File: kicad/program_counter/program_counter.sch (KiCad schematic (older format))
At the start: 34 parts, among them J1 DB37_Male, U76 SN74ALVC00

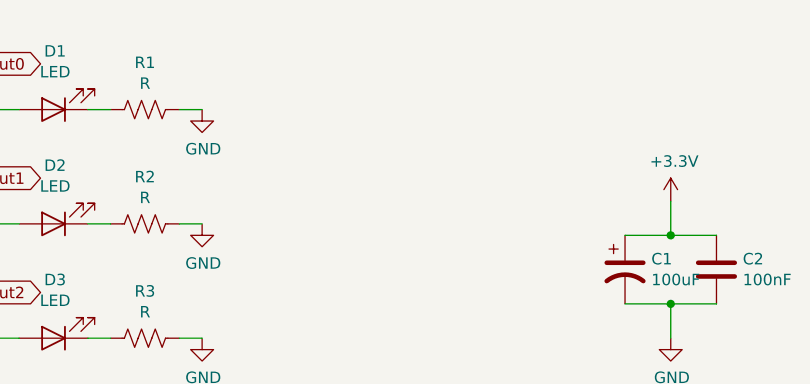
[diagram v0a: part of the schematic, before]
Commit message: ALU schematic, layout, routing complete. Associated motherboardmod. Also added Load LED to register and program counter boards.
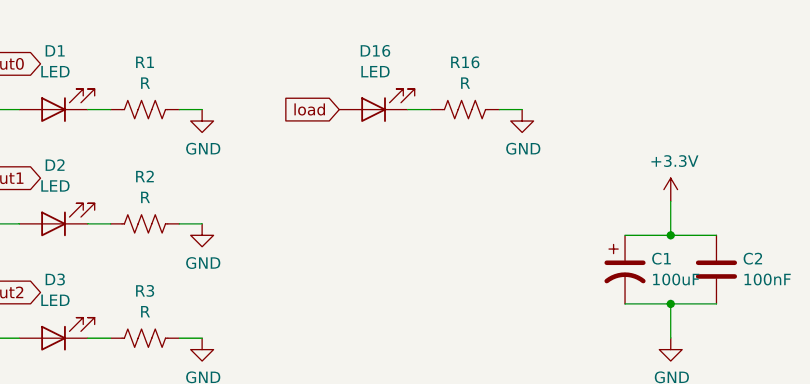
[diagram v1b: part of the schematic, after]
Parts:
- added D16: LED, LED_THT:LED_D5.0mm, symbol Device:LED
- added R16: R, Resistor_SMD:R_1206_3216Metric, symbol Device:R_US
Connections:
- net GND: now also R16.1
- net load: now also D16.2 (A)
- new net: D16.1 (K), R16.2
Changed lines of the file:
@@
 Wire Wire Line
 	7800 3350 7800 3200
+$Comp
+L Device:LED D16
+U 1 1 5EB18DDF
+P 6450 900
+F 0 "D16" H 6443 645 50  0000 C CNN
+F 1 "LED" H 6443 736 50  0000 C CNN
+F 2 "LED_THT:LED_D5.0mm" H 6450 900 50  0001 C CNN
+F 3 "~" H 6450 900 50  0001 C CNN
+	1    6450 900
+	-1   0    0    1
+$EndComp
+$Comp
+L Device:R_US R16
+U 1 1 5EB18DE5
+P 6850 900
+F 0 "R16" V 6645 900 50  0000 C CNN
+F 1 "R" V 6736 900 50  0000 C CNN
+F 2 "Resistor_SMD:R_1206_3216Metric" V 6780 900 50  0001 C CNN
+F 3 "~" H 6850 900 50  0001 C CNN
+	1    6850 900
+	0    1    1    0
+$EndComp
+Wire Wire Line
+	6600 900  6700 900
+$Comp
+L power:GND #PWR0172
+U 1 1 5EB18DEC
+P 7100 900
+F 0 "#PWR0172" H 7100 650 50  0001 C CNN
+F 1 "GND" H 7105 727 50  0000 C CNN
+F 2 "" H 7100 900 50  0001 C CNN
+F 3 "" H 7100 900 50  0001 C CNN
+	1    7100 900
+	1    0    0    -1
+$EndComp
+Wire Wire Line
+	7000 900  7100 900
+Text GLabel 6300 900  0    50   Input ~ 0
+load
 $EndSCHEMATC

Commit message: Readme updates (#6)
* Readme intro section

* Board revisions for manufacturing, add digikey PNs to all, added logo.
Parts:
- J1: footprint Connector_Dsub:DSUB-37_Male_Horizontal_P2.77x2.84mm_EdgePinOffset4.94mm_Housed_MountingHolesOffset7.48mm -> Connector_Dsub:DSUB-37_Male_Horizontal_P2.77x2.84mm_EdgePinOffset7.70mm_Housed_MountingHolesOffset9.12mm; Digikey PN (none) -> AE10986-ND
- R1, R10, R11, R12, R13, R14, R15, R16, R2, R3, R4, R5, R6, R7, R8, R9: value R -> 1K; Digikey PN (none) -> P1.0KECT-ND
- U76: Digikey PN (none) -> 296-5104-1-ND
